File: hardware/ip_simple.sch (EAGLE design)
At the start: 32 parts, among them Q4 irml9301, Q7 irml9301, T1 BC846, T3 BC846, Y1 32768Hz CFPX-217 12.5pF

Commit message: rev 2
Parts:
- removed C17: 100nF, rcl:C-EUC0805
- removed JP2: prog, SparkFun-Connectors:M06SIP_LOCK
- added C1: 100nF, rcl:C-EUC0805
- added U$2: MOLEX_6VERTICAL, Simplex-Connectors:MOLEX_6VERTICAL
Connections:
- removed net P6.2: C18.1, R22.2, R24.1, U$1.3
- new net P1.1: C18.1, R22.2, R24.1, U$1.15
- net GND: now also C1.2, U$2.1; no longer C17.1, JP2.1
- net N$4: now also C1.1
- net RST: now also U$2.2; no longer JP2.2
- net RX: now also U$2.5; no longer JP2.5
- net TEST: now also U$2.3; no longer JP2.3
- net TX: now also U$2.6; no longer JP2.6
- net VCC: now also U$2.4; no longer C17.2, JP2.4
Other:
- note added: "02"
- note removed: "01"

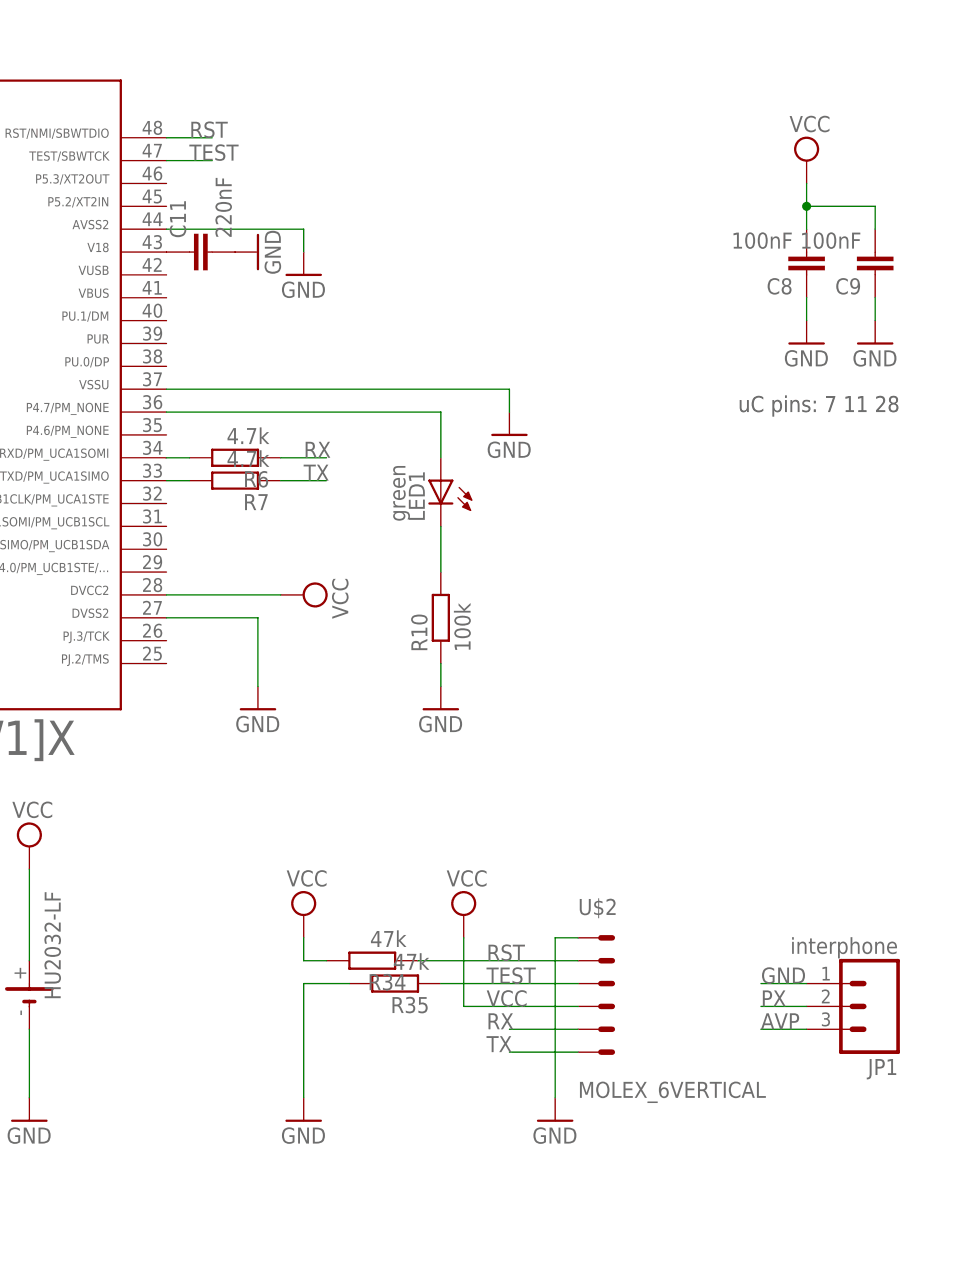
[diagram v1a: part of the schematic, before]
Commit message: cleanup for unused pins
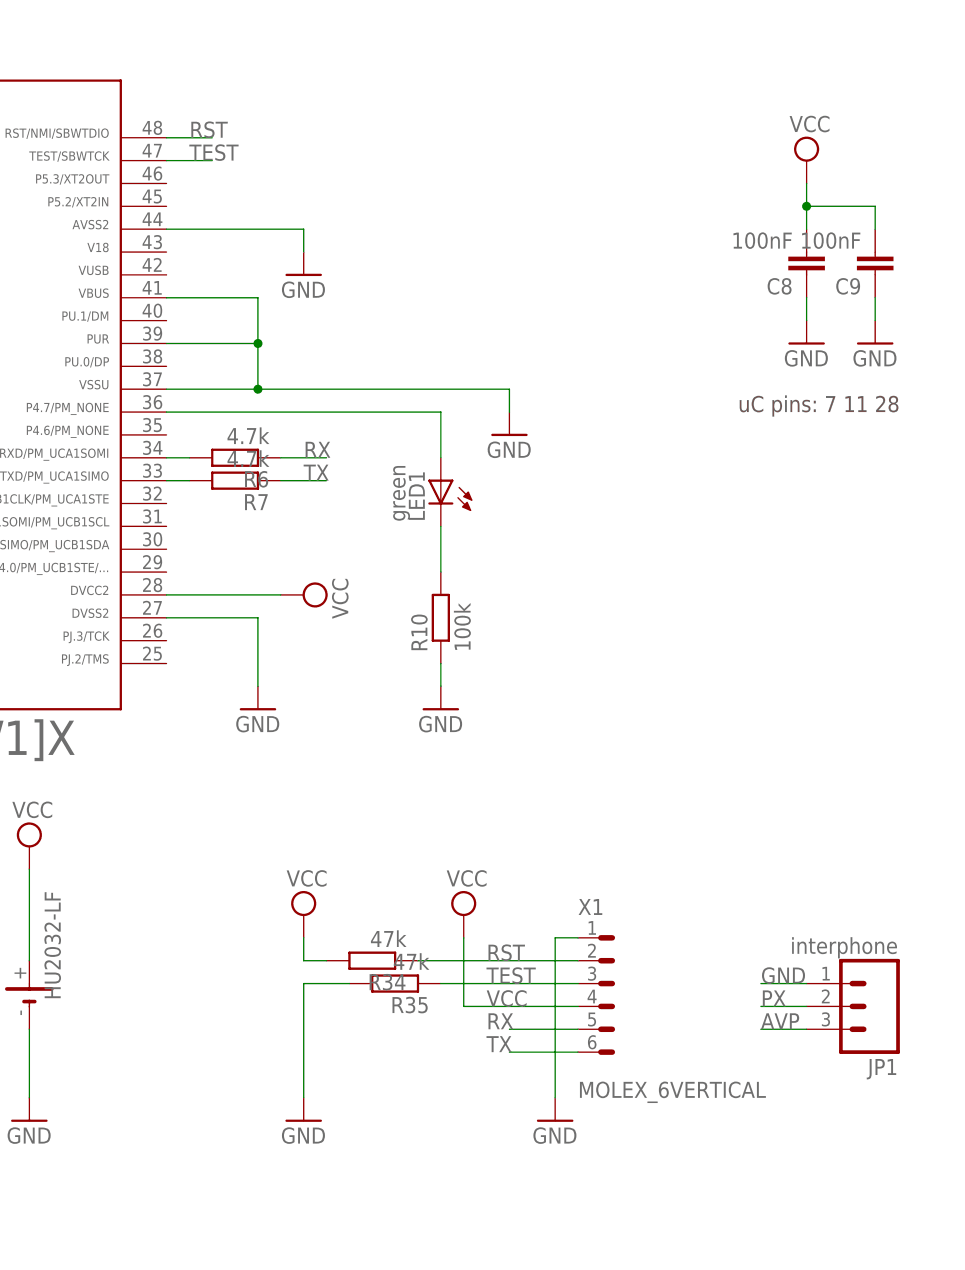
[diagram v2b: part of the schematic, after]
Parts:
- removed C11: 220nF, rcl:C-EUC0805
- removed U$2: MOLEX_6VERTICAL, Simplex-Connectors:MOLEX_6VERTICAL
- added X1: MOLEX_6VERTICAL, Simplex-Connectors:MOLEX_6VERTICAL
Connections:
- removed net N$7: C11.1, U$1.43
- net GND: now also U$1.39, U$1.41, X1.1; no longer C11.2, U$2.1
- net RST: now also X1.2; no longer U$2.2
- net RX: now also X1.5; no longer U$2.5
- net TEST: now also X1.3; no longer U$2.3
- net TX: now also X1.6; no longer U$2.6
- net VCC: now also X1.4; no longer U$2.4
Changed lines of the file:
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@@
 <layers>
 <layer number="1" name="Top" color="4" fill="1" visible="no" active="no"/>
+<layer number="2" name="Route2" color="1" fill="3" visible="no" active="no"/>
+<layer number="3" name="Route3" color="4" fill="3" visible="no" active="no"/>
+<layer number="14" name="Route14" color="1" fill="6" visible="no" active="no"/>
+<layer number="15" name="Route15" color="4" fill="6" visible="no" active="no"/>
 <layer number="16" name="Bottom" color="1" fill="1" visible="no" active="no"/>
 <layer number="17" name="Pads" color="2" fill="1" visible="no" active="no"/>
@@
 <part name="GND22" library="SparkFun" deviceset="GND" device=""/>
 <part name="C10" library="rcl" deviceset="C-EU" device="C0805" value="470nF"/>
-<part name="C11" library="rcl" deviceset="C-EU" device="C0805" value="220nF"/>
-<part name="GND23" library="SparkFun" deviceset="GND" device=""/>
 <part name="GND24" library="SparkFun" deviceset="GND" device=""/>
 <part name="R6" library="rcl" deviceset="R-EU_" device="R0805W" value="4.7k"/>
@@
 <part name="R2" library="rcl" deviceset="R-EU_" device="R0805W" value="2k2"/>
 <part name="JP1" library="SparkFun-Connectors" deviceset="M03" device="PTH" value="interphone"/>
-<part name="U$2" library="Simplex-Connectors" deviceset="MOLEX_6" device="VERTICAL"/>
 <part name="C1" library="rcl" deviceset="C-EU" device="C0805" value="100nF"/>
 <part name="GND2" library="SparkFun" deviceset="GND" device=""/>
+<part name="X1" library="Simplex-Connectors" deviceset="MOLEX_6" device="VERTICAL"/>
 </parts>
 <sheets>
@@
 <instance part="GND22" gate="1" x="160.02" y="127"/>
 <instance part="C10" gate="G$1" x="160.02" y="134.62"/>
-<instance part="C11" gate="G$1" x="226.06" y="154.94" rot="R90"/>
-<instance part="GND23" gate="1" x="233.68" y="154.94" rot="R90"/>
 <instance part="GND24" gate="1" x="261.62" y="134.62"/>
 <instance part="R6" gate="G$1" x="231.14" y="132.08" rot="R180"/>
@@
 <instance part="R2" gate="G$1" x="99.06" y="121.92" rot="R90"/>
 <instance part="JP1" gate="G$1" x="302.26" y="71.12" rot="R180"/>
-<instance part="U$2" gate="G$1" x="269.24" y="60.96"/>
 <instance part="C1" gate="G$1" x="99.06" y="91.44"/>
 <instance part="GND2" gate="1" x="99.06" y="78.74"/>
+<instance part="X1" gate="G$1" x="271.78" y="73.66"/>
 </instances>
 <busses>
@@
 </segment>
 <segment>
-<pinref part="C11" gate="G$1" pin="2"/>
-<pinref part="GND23" gate="1" pin="GND"/>
-</segment>
-<segment>
 <pinref part="U$1" gate="G$1" pin="37"/>
 <pinref part="GND24" gate="1" pin="GND"/>
-<wire x1="223.52" y1="139.7" x2="261.62" y2="139.7" width="0.1524" layer="91"/>
+<wire x1="223.52" y1="139.7" x2="233.68" y2="139.7" width="0.1524" layer="91"/>
+<wire x1="233.68" y1="139.7" x2="261.62" y2="139.7" width="0.1524" layer="91"/>
 <wire x1="261.62" y1="139.7" x2="261.62" y2="137.16" width="0.1524" layer="91"/>
+<pinref part="U$1" gate="G$1" pin="41"/>
+<wire x1="223.52" y1="149.86" x2="233.68" y2="149.86" width="0.1524" layer="91"/>
+<wire x1="233.68" y1="149.86" x2="233.68" y2="144.78" width="0.1524" layer="91"/>
+<pinref part="U$1" gate="G$1" pin="39"/>
+<wire x1="233.68" y1="144.78" x2="233.68" y2="139.7" width="0.1524" layer="91"/>
+<wire x1="223.52" y1="144.78" x2="233.68" y2="144.78" width="0.1524" layer="91"/>
+<junction x="233.68" y="144.78"/>
+<junction x="233.68" y="139.7"/>
 </segment>
 <segment>
@@
 <wire x1="269.24" y1="78.74" x2="266.7" y2="78.74" width="0.1524" layer="91"/>
 <wire x1="266.7" y1="78.74" x2="266.7" y2="60.96" width="0.1524" layer="91"/>
-<pinref part="U$2" gate="G$1" pin="1"/>
+<pinref part="X1" gate="G$1" pin="1"/>
 </segment>
 <segment>
@@
 </segment>
 </net>
-<net name="N$7" class="0">
-<segment>
-<pinref part="U$1" gate="G$1" pin="43"/>
-<pinref part="C11" gate="G$1" pin="1"/>
-</segment>
-</net>
 <net name="N$11" class="0">
 <segment>
@@
 <wire x1="269.24" y1="68.58" x2="261.62" y2="68.58" width="0.1524" layer="91"/>
 <label x="259.08" y="68.58" size="1.778" layer="95"/>
-<pinref part="U$2" gate="G$1" pin="5"/>
+<pinref part="X1" gate="G$1" pin="5"/>
 </segment>
 </net>
@@
 <wire x1="269.24" y1="66.04" x2="261.62" y2="66.04" width="0.1524" layer="91"/>
 <label x="259.08" y="66.04" size="1.778" layer="95"/>
-<pinref part="U$2" gate="G$1" pin="6"/>
+<pinref part="X1" gate="G$1" pin="6"/>
 </segment>
 </net>
@@
 <wire x1="269.24" y1="71.12" x2="256.54" y2="71.12" width="0.1524" layer="91"/>
 <label x="259.08" y="71.12" size="1.778" layer="95"/>
-<pinref part="U$2" gate="G$1" pin="4"/>
+<pinref part="X1" gate="G$1" pin="4"/>
 </segment>
 <segment>
@@
 <pinref part="R34" gate="G$1" pin="1"/>
 <wire x1="251.46" y1="76.2" x2="269.24" y2="76.2" width="0.1524" layer="91"/>
-<pinref part="U$2" gate="G$1" pin="2"/>
+<pinref part="X1" gate="G$1" pin="2"/>
 </segment>
 </net>
@@
 <label x="259.08" y="73.66" size="1.778" layer="95"/>
 <pinref part="R35" gate="G$1" pin="1"/>
-<pinref part="U$2" gate="G$1" pin="3"/>
-</segment>
-</net>
+<pinref part="X1" gate="G$1" pin="3"/>
+</segment>
+</net>
